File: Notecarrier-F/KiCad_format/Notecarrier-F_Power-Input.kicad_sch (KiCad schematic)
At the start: 20 parts, among them J1 S2BPHSM4TBLFSN, J2 S2BPHSM4TBLFSN, J3 S2BPHSM4TBLFSN, J4 10118193-0001LF, U2 BQ24210DQCT

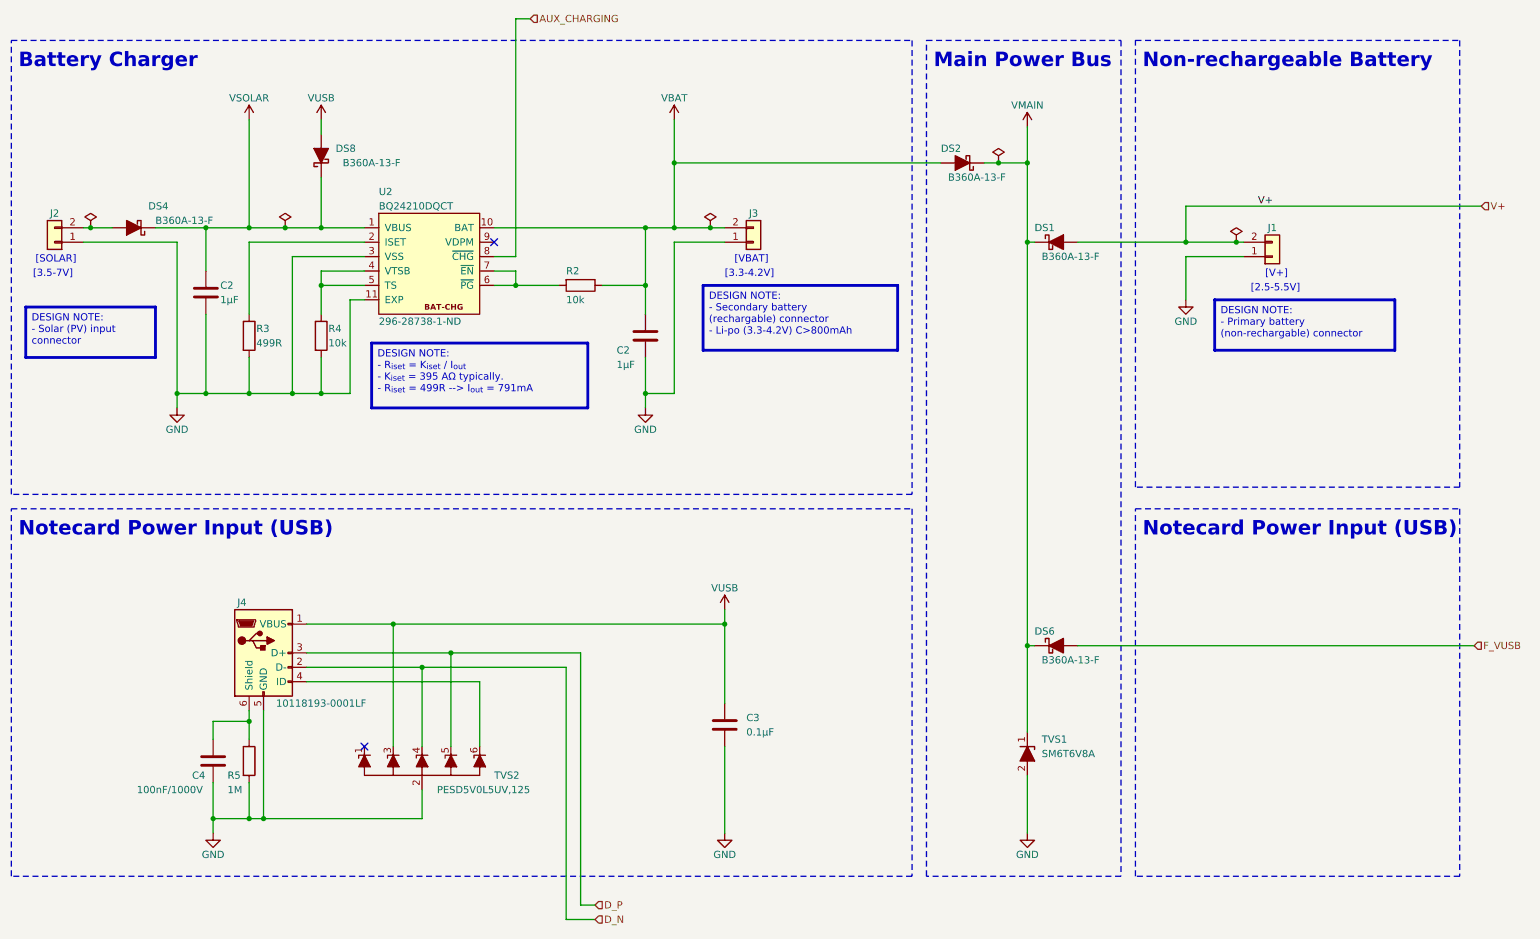
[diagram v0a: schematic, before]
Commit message: Complete first pass PCB rev B.
See README for details. Ready to start Validation.
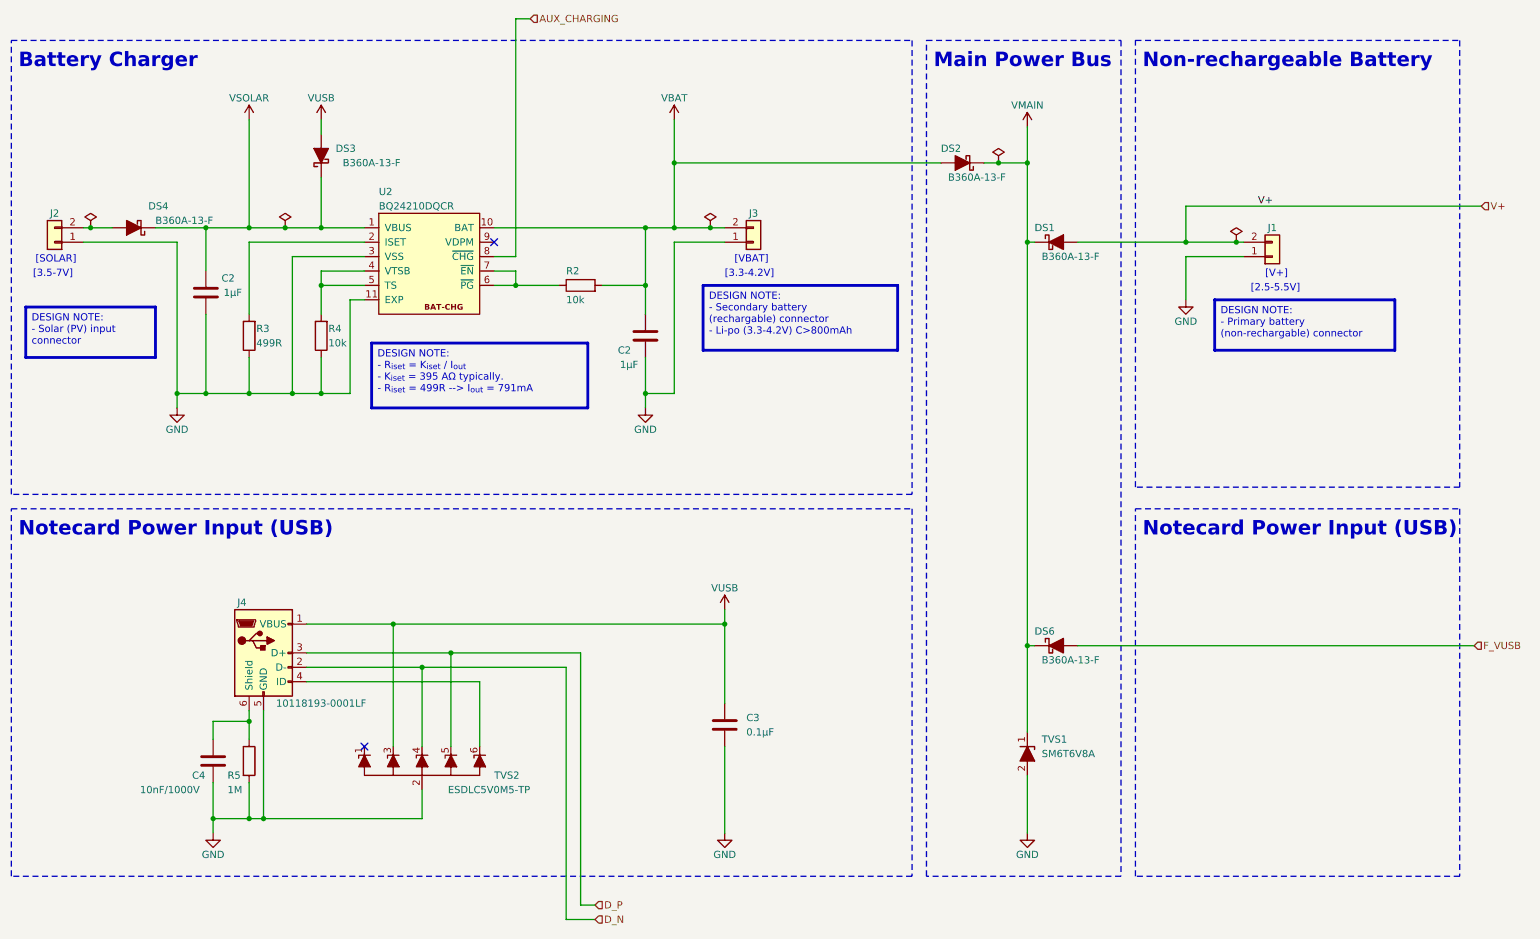
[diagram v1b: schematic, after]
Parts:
- C2: footprint blues-kicad-lib:CAP 0402_1005 -> blues-kicad-lib:C-0603_Fv1.2; Datasheet 2 (none) -> https://datasheet.octopart.com/0603YC105KAT2A-KYOCERA-AVX-d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; Design Description (none) -> Capacitor ceramic 1u ±10% X5R 25V; Design MPN (none) -> CC0603KRX5R8BB105; Design Manufacturer (none) -> Yageo; Design Order Code (none) -> 311-1445-1-ND; Design Supplier (none) -> Digi-Key; MPN (none) -> CC0603KRX7R7BB105; MPN 2 (none) -> 0603YC105KAT2A; Manufacturer Samsung -> Yageo; Manufacturer 2 (none) -> AVX; Mfr Description (none) -> 0603 1 uF 16 V ±10 % Tolerance X7R SMT Multilayer Ceramic C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; Mfr Description 2 (none) -> 0603 1000nF Ceramic Multilayer Capacitor; 16 VDC; +125degC;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; Order Code 1276-1067-1-ND -> (none); Part Number CL05A105KO5NNNC -> (none); Supplier Digi-Key -> (none)
- C3: footprint blues-kicad-lib:CAP 0402_1005 -> blues-kicad-lib:C-0402_Fv1.2; Datasheet 2 (none) -> http://datasheet.octopart.com/CL05B104KO5NNNC-Samsung-Elect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; Datasheet 3 (none) -> https://datasheet.octopart.com/GRM155R71C104KA88D-Murata-da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; Design Description (none) -> Capacitor ceramic 100n ±10% X7R 16V 0402; Design MPN (none) -> N/A; Design Manufacturer (none) -> N/A; Design Order Code (none) -> 490-3261-1-ND; Design Supplier (none) -> Digi-Key; MPN (none) -> CC0402KRX7R7BB104; MPN 2 (none) -> CL05B104KO5NNNC; MPN 3 (none) -> GRM155R71C104KA88D; Manufacturer Samsung -> Yageo; Manufacturer 2 (none) -> Samsung; Manufacturer 3 (none) -> Murata; Mfr Description (none) -> 0402 0.1 uF 16 V ±10 % Tolerance X7R SMT Multilayer Ceramic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; Mfr Description 2 (none) -> Ceramic capacitor SMD-0402 100nF /16V X7R# K +-10%, Samsung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; Mfr Description 3 (none) -> Multilayer Ceramic Capacitor, 0.1 uF, 16 V, ± 10%, X7R, 040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; Order Code 187-CL05B104KO5NNNC -> (none); Part Number CL05B104KO5NNNC -> (none); Supplier Farnell -> (none)
- C4: value 100nF/1000V -> 10nF/1000V; footprint blues-kicad-lib:CAP 1206_3216 - 0.8MM -> blues-kicad-lib:C-1206_Fv1.2; Datasheet 2 (none) -> http://datasheet.octopart.com/1206B103K102CT-Walsin-Technol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; Datasheet 3 (none) -> http://datasheet.octopart.com/CS1206KKX7RCBB103-Yageo-datas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; Design Description (none) -> Capacitor ceramic 10n ±10% X7R 1000V 1206; Design MPN (none) -> CS1206KKX7RCBB103; Design Manufacturer (none) -> YAGEO; Design Order Code (none) -> 311-3578-1-ND; Design Supplier (none) -> Digi-Key; MPN (none) -> C1206C103KDRACTU; MPN 2 (none) -> 1206B103K102CT; MPN 3 (none) -> CS1206KKX7RCBB103; Manufacturer Yageo -> KEMET; Manufacturer 2 (none) -> Walsin Technologies; Manufacturer 3 (none) -> Yageo; Mfr Description (none) -> Cap Ceramic 0.01uF 1000V X7R 10% Pad SMD 1206 125C Automoti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; Mfr Description 2 (none) -> Chip Capacitor 1206 MLCC X7R 0.01 uF+/- 10% 1K V T&R MH; Mfr Description 3 (none) -> Cap Ceramic 0.01uF 1000V X7R 10% Pad SMD 1206 Soft Terminat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; Order Code 311-3578-1-ND -> (none); Part Number CS1206KKX7RCBB103 -> (none); Supplier Digi-Key -> (none)
- DS1, DS2, DS4, DS6: footprint (none) -> blues-kicad-lib:DO-214AC SMA_Fv1.2; symbol Device:D_Schottky_Filled -> blues-kicad-lib:D_Schottky_Filled_Swapped; Design Description (none) -> Schottky Diode B360-13-F 60V/3A; Design MPN (none) -> B360A-13-F; Design Manufacturer (none) -> Diodes Inc; Design Order Code (none) -> B360A-FDICT-ND; Design Supplier (none) -> Digi-Key; MPN (none) -> B360A-13-F; Manufacturer (none) -> Diodes Inc.; Mfr Description (none) -> Rectifier Diode, Schottky, 1 Phase, 1 Element, 3A, 60V V(RR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
- DS3: renamed from DS8; footprint (none) -> blues-kicad-lib:DO-214AC SMA_Fv1.2; symbol Device:D_Schottky_Filled -> blues-kicad-lib:D_Schottky_Filled_Swapped; Design Description (none) -> Schottky Diode B360-13-F 60V/3A; Design MPN (none) -> B360A-13-F; Design Manufacturer (none) -> Diodes Inc; Design Order Code (none) -> B360A-FDICT-ND; Design Supplier (none) -> Digi-Key; MPN (none) -> B360A-13-F; Manufacturer (none) -> Diodes Inc.; Mfr Description (none) -> Rectifier Diode, Schottky, 1 Phase, 1 Element, 3A, 60V V(RR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
- J1, J2, J3: footprint blues-kicad-lib:JST S2B-PH-SM4-TB -> blues-kicad-lib:JST S2B-PH-SM4-TB_Fv1.2; Datasheet 2 (none) -> https://www.jst-mfg.com/product/pdf/eng/ePH.pdf; Datasheet 3 (none) -> https://www.adafruit.com/product/1769; Design Description (none) -> PH SMT SIDE ENTRY HDR 2W; Design MPN (none) -> S2BPHSM4TBLFSN; Design Manufacturer (none) -> JST; Design Order Code (none) -> 455-1749-1-ND; Design Supplier (none) -> Digi-Key; MPN (none) -> 20404; MPN 2 (none) -> S2B-PH-SM4-K-TBT(LF)(SN); MPN 3 (none) -> 1769; Manufacturer JST -> 4UCON; Manufacturer 2 (none) -> JST Sales America Inc.; Manufacturer 3 (none) -> Adafruit; Mfr Description (none) -> 2.0MM JST PH SERIES EQUIVALENT WAFER 02P SMT 90° WITHOUT PO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; Mfr Description 2 (none) -> Connector Header Surface Mount, Right Angle 2 position 0.07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; Mfr Description 3 (none) -> JST-PH 2-Pin SMT Right Angle Connector; Order Code 455-1749-1-ND -> (none); Part Number S2B-PH-SM4-TB(LF)(SN -> (none); Supplier Digi-Key -> (none)
- J4: footprint blues-kicad-lib:FCI USB 10118193-0001LF -> blues-kicad-lib:FCI USB 10118193-0001LF_Fv1.2; Design Description (none) -> CONN RCPT USB2.0 MICRO B SMD R/A; Design MPN (none) -> 10118193-0001LF; Design Manufacturer (none) -> Amphenol ICC (FCI); Design Order Code (none) -> 609-4616-2-ND; Design Supplier (none) -> Digi-Key; MPN (none) -> 10118193-0001LF; Order Code 609-4616-2-ND -> (none); Part Number 10118193-0001LF -> (none); Supplier Digi-Key -> (none)
- R2, R4: footprint blues-kicad-lib:RES 0402_1005 -> blues-kicad-lib:R-0402_Fv1.2; Datasheet 2 (none) -> http://datasheet.octopart.com/RC0402FR-0710KL-Yageo-datashe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; Datasheet 3 (none) -> https://datasheet.octopart.com/ERJ-2RKF1002X-Panasonic-data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; Design Description (none) -> Resistor 10k ±1% 0402; Design MPN (none) -> N/A; Design Manufacturer (none) -> N/A; Design Order Code (none) -> 311-10.0KLRCT-ND; Design Supplier (none) -> Digi-Key; MPN (none) -> RC1005F103CS; MPN 2 (none) -> RC0402FR-0710KL; MPN 3 (none) -> ERJ-2RKF1002X; Manufacturer 2 (none) -> Yageo; Manufacturer 3 (none) -> Panasonic; Mfr Description (none) -> Res Thick Film 0402 10K Ohm 1% 1/16W ±100ppm/°C Molded SMD 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; Mfr Description 2 (none) -> Res General Purpose Thick Film 0402 10K Ohm 1% 1/16W ±100pp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; Mfr Description 3 (none) -> Res Thick Film 0402 10K Ohm 1% 1/10W ±100ppm/°C Molded SMD 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; Order Code 1276-3431-2-ND -> (none); Part Number RC1005F103CS -> (none); Supplier Digi-Key -> (none)
- R3: footprint blues-kicad-lib:RES 0402_1005 -> blues-kicad-lib:R-0402_Fv1.2; Datasheet 2 (none) -> https://datasheet.octopart.com/CR0402-FX-4990GLF-Bourns-dat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; Datasheet 3 (none) -> https://datasheet.octopart.com/RC0402FR-07499RP-Yageo-datas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; Design Description (none) -> Resistor 499R ±1% 0402; Design MPN (none) -> N/A; Design Manufacturer (none) -> N/A; MPN (none) -> 0402WGF4990TCE; MPN 2 (none) -> CR0402-FX-4990GLF; MPN 3 (none) -> RC0402FR-07499RP; Manufacturer (none) -> Royal Ohm; Manufacturer 2 (none) -> Bourns; Manufacturer 3 (none) -> Yageo; Mfr Description (none) -> Res Thick Film 0402 499 Ohm 1% 0.063W(1/16W) ±100ppm/°C Pad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; Mfr Description 2 (none) -> SMD Chip Resistor, 499 Ohm, ± 1%, 63 mW, 0402 [1005 Metric]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; Mfr Description 3 (none) -> Res General Purpose Thick Film 0402 499 Ohm 1% 1/16W ±100pp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
- R5: footprint blues-kicad-lib:RES 1206_3216 -> blues-kicad-lib:R-1206_Fv1.2; Datasheet 2 (none) -> http://datasheet.octopart.com/CRCW12061M00FKEA-Vishay-datas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; Datasheet 3 (none) -> https://datasheet.octopart.com/RC1206FR-071ML-Yageo-datashe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; Datasheet 4 (none) -> https://datasheet.octopart.com/CRCW12061M00FKEAC-Vishay-dat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; Design Description (none) -> Resistor 1M ±1% 1206; Design MPN (none) -> N/A; Design Manufacturer (none) -> N/A; MPN (none) -> CR1206-FX-1004ELF; MPN 2 (none) -> CRCW12061M00FKEA; MPN 3 (none) -> RC1206FR-071ML; MPN 4 (none) -> CRCW12061M00FKEAC; Manufacturer Yageo -> Bourns; Manufacturer 2 (none) -> Vishay; Manufacturer 3 (none) -> Yageo; Manufacturer 4 (none) -> Vishay; Mfr Description (none) -> Res Thick Film 1206 1M Ohm 1% 1/4W ±100ppm/°C Molded SMD SM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; Mfr Description 2 (none) -> Res Thick Film 1206 1M Ohm 1% 1/4W ±100ppm/°C Molded SMD SM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; Mfr Description 3 (none) -> Res Thick Film 1206 1M Ohm 1% 0.25W(1/4W) ±100ppm/C Pad SMD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; Mfr Description 4 (none) -> Res Thick Film 1206 1M Ohm 1% 1/4W ±100ppm/°C Molded SMD Pa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; Order Code 311-1.00MFRTR-ND -> (none); Part Number RC1206FR-071ML -> (none); Supplier Digi-Key -> (none)
- TVS1: footprint blues-kicad-lib:SMB_Backwards -> blues-kicad-lib:SMB_Fv1.2; Design Description (none) -> DIODO TVS TRANSIL UNIDIR. 600W 6.8V SM6T6V8A SMB SMT; Design MPN (none) -> SM6T6V8A; Design Manufacturer (none) -> STMicroelectronics; Design Order Code (none) -> 497-6501-1-ND; Design Supplier (none) -> Digi-Key; MPN (none) -> SM6T6V8A; Mfr Description (none) -> SM6T Series 600 W 6.8 V Uni Directional Transient Voltage S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; Order Code 6871072 -> (none); Part Number SM6T6V8A -> (none); Supplier RSComponents -> (none)
- TVS2: value PESD5V0L5UV,125 -> ESDLC5V0M5-TP; footprint blues-kicad-lib:SOT666 -> blues-kicad-lib:SOT666_Fv1.2; Datasheet 2 (none) -> http://datasheet.octopart.com/PESD5V0L5UV%2C115-Nexperia-da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; Datasheet 3 (none) -> http://datasheet.octopart.com/PESD5V0L5UV%2C125-Nexperia-da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; Design Description (none) -> PESD Series 25 W 5 V Uni-Directional Fivefold ESD Protectio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; Design MPN (none) -> PESD5V0L5UV,125; Design Manufacturer (none) -> Nexperia; Design Order Code (none) -> 1727-5797-1-ND; Design Supplier (none) -> Digi-Key; MPN (none) -> ESDLC5V0M5-TP; MPN 2 (none) -> PESD5V0L5UV,115; MPN 3 (none) -> PESD5V0L5UV,125; Manufacturer Nexperia -> MCC; Manufacturer 2 (none) -> Nexperia; Manufacturer 3 (none) -> Nexperia; Mfr Description (none) -> ESD Suppressors / TVS Diodes 5V ESD Protection Devices; Mfr Description 2 (none) -> PESD5V0L5UV - Low capacitance unidirectional fivefold ESD p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; Mfr Description 3 (none) -> PESD5V0L5UV - Low capacitance unidirectional fivefold ESD p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; Order Code 1727-5797-1-ND -> (none); Part Number PESD5V0L5UV125 -> (none); Supplier Digi-Key -> (none)
- U2: value BQ24210DQCT -> BQ24210DQCR; footprint blues-kicad-lib:BQ24210DQCT -> blues-kicad-lib:WSON10-EXP_Fv1.2; Datasheet 2 (none) -> https://octopart.com/opatz8j6/c1?t=7-wFuY1_ByudSAAsJC5ycWYT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; Design Description (none) -> INTEGRATO BQ24210DQCT WSON10 TEXAS SMT; Design MPN (none) -> BQ24210DQCT; Design Manufacturer (none) -> Texas Instruments; Design Order Code (none) -> 296-28738-1-ND; Design Supplier (none) -> Digi-Key; MPN (none) -> BQ24210DQCR; MPN 2 (none) -> BQ24210DQCT; Manufacturer 2 (none) -> Texas Instruments; Mfr Description (none) -> 800mA, single-input, single cell Li-ion Solar battery charg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; Mfr Description 2 (none) -> 800mA, single-input, single cell Li-ion Solar battery charg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; Order Code 296-28738-1-ND -> (none); Part Number BQ24210DQCT -> (none); Supplier Digi-Key -> (none)
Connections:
- net F_VUSB: now also DS6.1 (A); no longer DS6.2 (A)
- net GND: now also C2.1, C2.1, C3.2, R3.1, R4.1; no longer C2.2, C2.2, C3.1, R3.2, R4.2
- net V+: now also DS1.1 (A); no longer DS1.2 (A)
- net VBAT: now also C2.2, DS2.1 (A), R2.2; no longer C2.1, DS2.2 (A), R2.1
- net VMAIN: now also DS1.2 (K), DS2.2 (K), DS6.2 (K); no longer DS1.1 (K), DS2.1 (K), DS6.1 (K)
- net VSOLAR: now also C2.2, DS3.2 (K), DS4.2 (K); no longer C2.1, DS3.1 (K), DS4.1 (K)
- net VUSB: now also C3.1, DS3.1 (A); no longer C3.2, DS3.2 (A)
- net at U2.2 (ISET): now also R3.2; no longer R3.1
- net at U2.4 (VTSB), U2.5 (TS): now also R4.2; no longer R4.1
- net at J2.2 (Pin_2): now also DS4.1 (A); no longer DS4.2 (A)
- net at U2.6 (~{PG}), U2.7 (~{EN}): now also R2.1; no longer R2.2
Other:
- moved on the sheet: C2, C3, R2, R3, R4

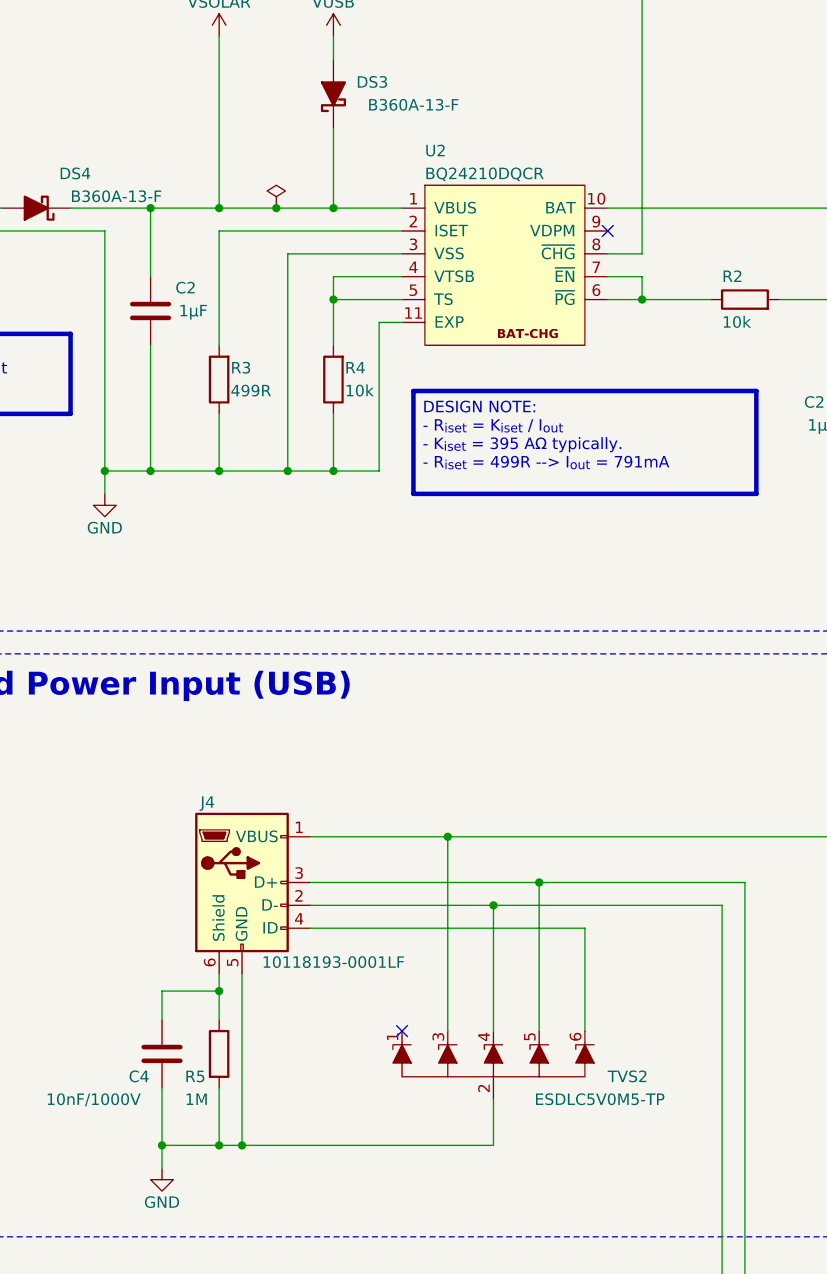
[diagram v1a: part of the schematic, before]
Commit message: Apply cosmetic tweaks from Validation activity.
- Remove 4 way junction.
- Remove off-grid connections.
- Correct visible component values
- Add missing design notes.
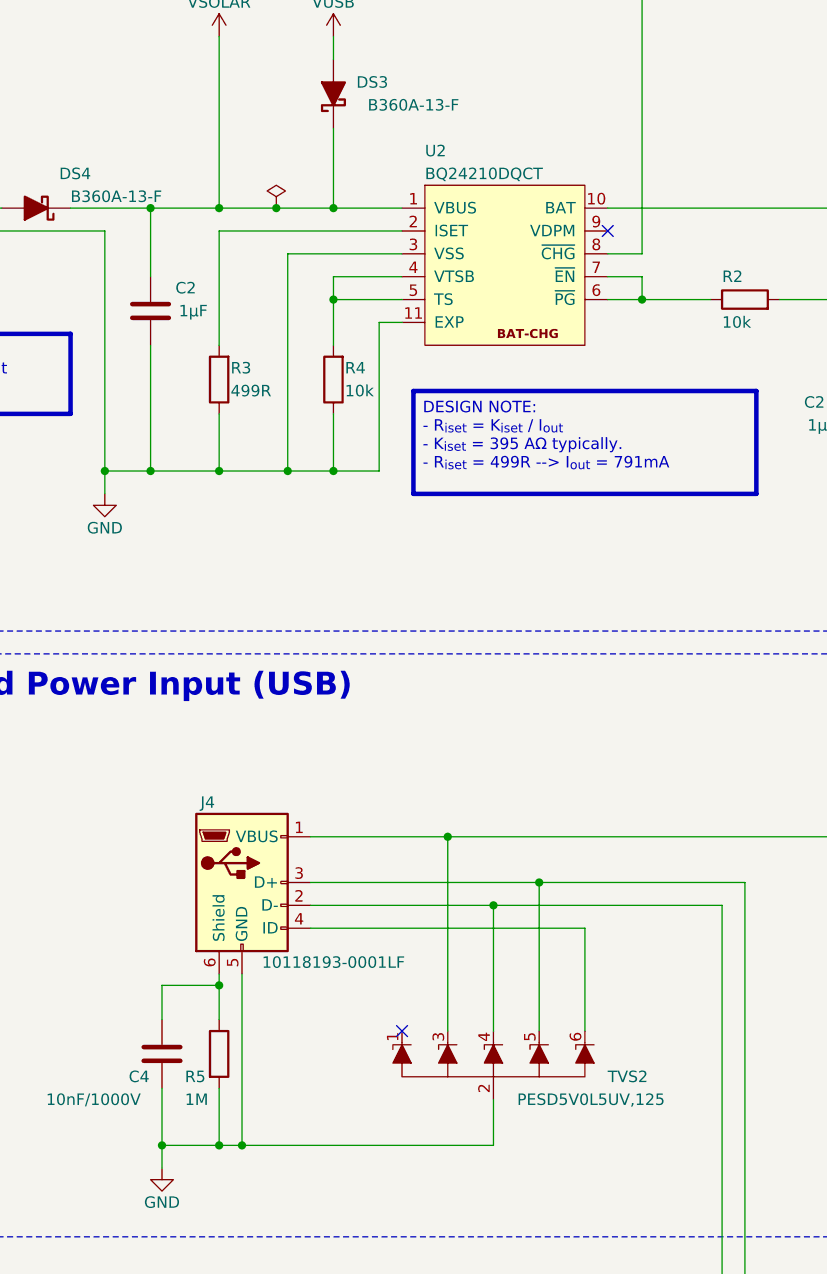
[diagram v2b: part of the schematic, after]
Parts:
- TVS2: value ESDLC5V0M5-TP -> PESD5V0L5UV,125
- U2: value BQ24210DQCR -> BQ24210DQCT
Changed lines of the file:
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@@
   (junction (at 132.08 44.45) (diameter 0) (color 0 0 0 0)
   )
-  (junction (at 57.15 142.875) (diameter 0) (color 0 0 0 0)
-  )
   (junction (at 138.43 55.88) (diameter 0) (color 0 0 0 0)
   )
@@
   )
   (junction (at 64.77 85.09) (diameter 0) (color 0 0 0 0)
+  )
+  (junction (at 57.15 142.24) (diameter 0) (color 0 0 0 0)
   )
   (junction (at 63.5 55.88) (diameter 0) (color 0 0 0 0)
@@
     (stroke (width 0) (type default))
   )
+  (wire (pts (xy 57.15 142.24) (xy 57.15 146.05))
+    (stroke (width 0) (type default))
+  )
+  (wire (pts (xy 50.8 142.24) (xy 50.8 146.05))
+    (stroke (width 0) (type default))
+  )
   (wire (pts (xy 57.15 153.67) (xy 57.15 160.02))
     (stroke (width 0) (type default))
@@
     (stroke (width 0) (type default))
   )
-  (wire (pts (xy 57.15 142.875) (xy 57.15 146.05))
-    (stroke (width 0) (type default))
-  )
   (wire (pts (xy 274.32 52.07) (xy 222.25 52.07))
     (stroke (width 0) (type default))
@@
     (stroke (width 0) (type default))
   )
-  (wire (pts (xy 50.8 142.875) (xy 57.15 142.875))
+  (wire (pts (xy 50.8 142.24) (xy 57.15 142.24))
     (stroke (width 0) (type default))
   )
@@
     (stroke (width 0) (type default))
   )
-  (wire (pts (xy 57.15 140.97) (xy 57.15 142.875))
+  (wire (pts (xy 57.15 140.97) (xy 57.15 142.24))
     (stroke (width 0) (type default))
   )
@@
   )
   (wire (pts (xy 69.85 66.04) (xy 69.85 71.12))
-    (stroke (width 0) (type default))
-  )
-  (wire (pts (xy 50.8 146.05) (xy 50.8 142.875))
     (stroke (width 0) (type default))
   )
@@
       (effects (font (size 1.27 1.27)) (justify left))
     )
-    (property "Value" "ESDLC5V0M5-TP" (at 106.68 154.94 0)
+    (property "Value" "PESD5V0L5UV,125" (at 106.68 154.94 0)
       (effects (font (size 1.27 1.27)) (justify right))
     )
@@
       (effects (font (size 1.27 1.27)) (justify left))
     )
-    (property "Value" "BQ24210DQCR" (at 80.01 52.07 0)
+    (property "Value" "BQ24210DQCT" (at 80.01 52.07 0)
       (effects (font (size 1.27 1.27)) (justify left))
     )

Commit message: Apply minor corrections from BOM validation.
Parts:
- J4: Manufacturer Amphenol ICC -> Amphenol ICC / FCI; Mfr Description (none) -> FCI Right Angle Surface Mount Mount Female USB Connector; 1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
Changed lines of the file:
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@@
       (effects (font (size 1.27 1.27)) hide)
     )
-    (property "Datasheet" "~" (at 63.5 132.08 0)
+    (property "Datasheet" "http://datasheet.octopart.com/10118193-0001LF-Amphenol-ICC-datasheet-96019471.pdf" (at 63.5 132.08 0)
       (effects (font (size 1.27 1.27)) hide)
     )
-    (property "Description" "CONN RCPT USB2.0 MICRO B SMD R/A" (at 59.69 130.81 0)
+    (property "Description" "CONN MICRO-B USB F RIGHT ANGLE WITH FLANGE AND 2 LEGS SMT" (at 59.69 130.81 0)
       (effects (font (size 1.27 1.27)) hide)
     )
-    (property "Manufacturer" "Amphenol ICC" (at 59.69 130.81 0)
+    (property "Manufacturer" "Amphenol ICC / FCI" (at 59.69 130.81 0)
       (effects (font (size 1.27 1.27)) hide)
     )
@@
       (effects (font (size 1.27 1.27)) hide)
     )
-    (property "Mfr Description" "" (at 59.69 130.81 0)
+    (property "Mfr Description" "FCI Right Angle Surface Mount Mount Female USB Connector; 100 V ac; 1.8A" (at 59.69 130.81 0)
       (effects (font (size 1.27 1.27)) hide)
     )
